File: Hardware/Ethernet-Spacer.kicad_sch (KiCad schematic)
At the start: 13 parts, among them J1 Conn_01x07_Male, J10 Conn_01x02_Male, J11 Conn_01x02_Male, J2 Conn_01x04_Male, J3 Conn_01x02_Male, J4 Conn_01x02_Male, J5 Conn_01x02_Male, J6 Conn_01x02_Male, J7 Conn_01x08_Male, J9 QWIIC_Stackable

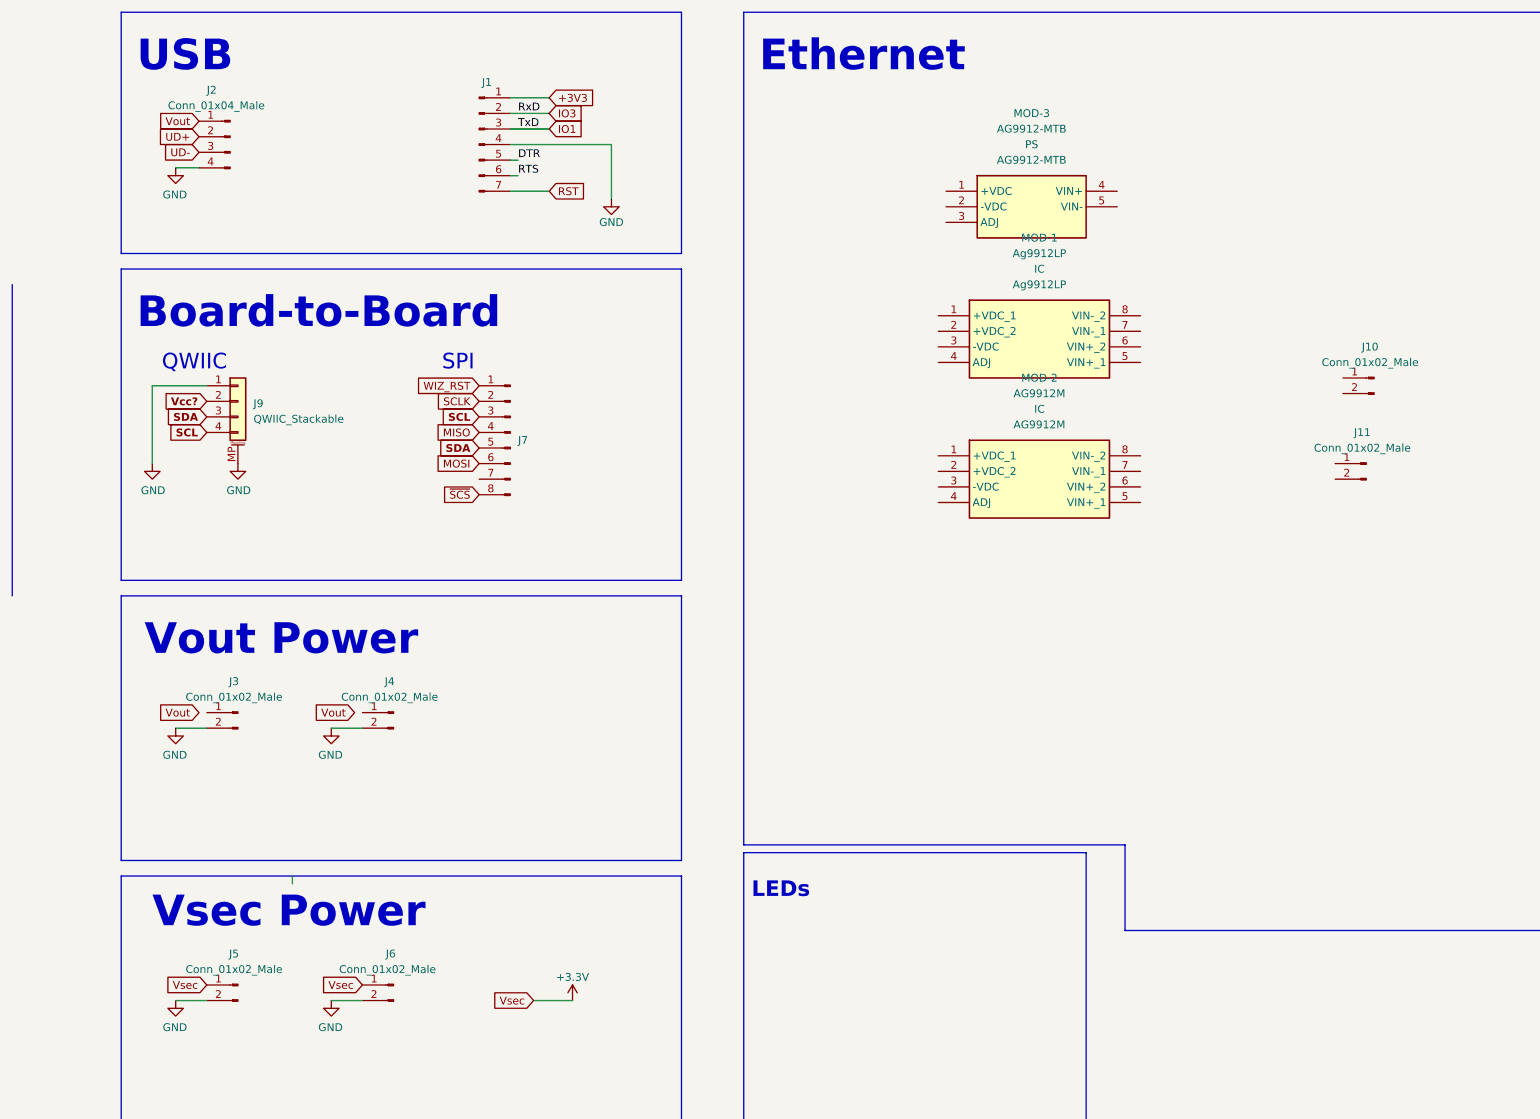
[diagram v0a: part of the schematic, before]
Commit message: Still working on changes to J7/J9...
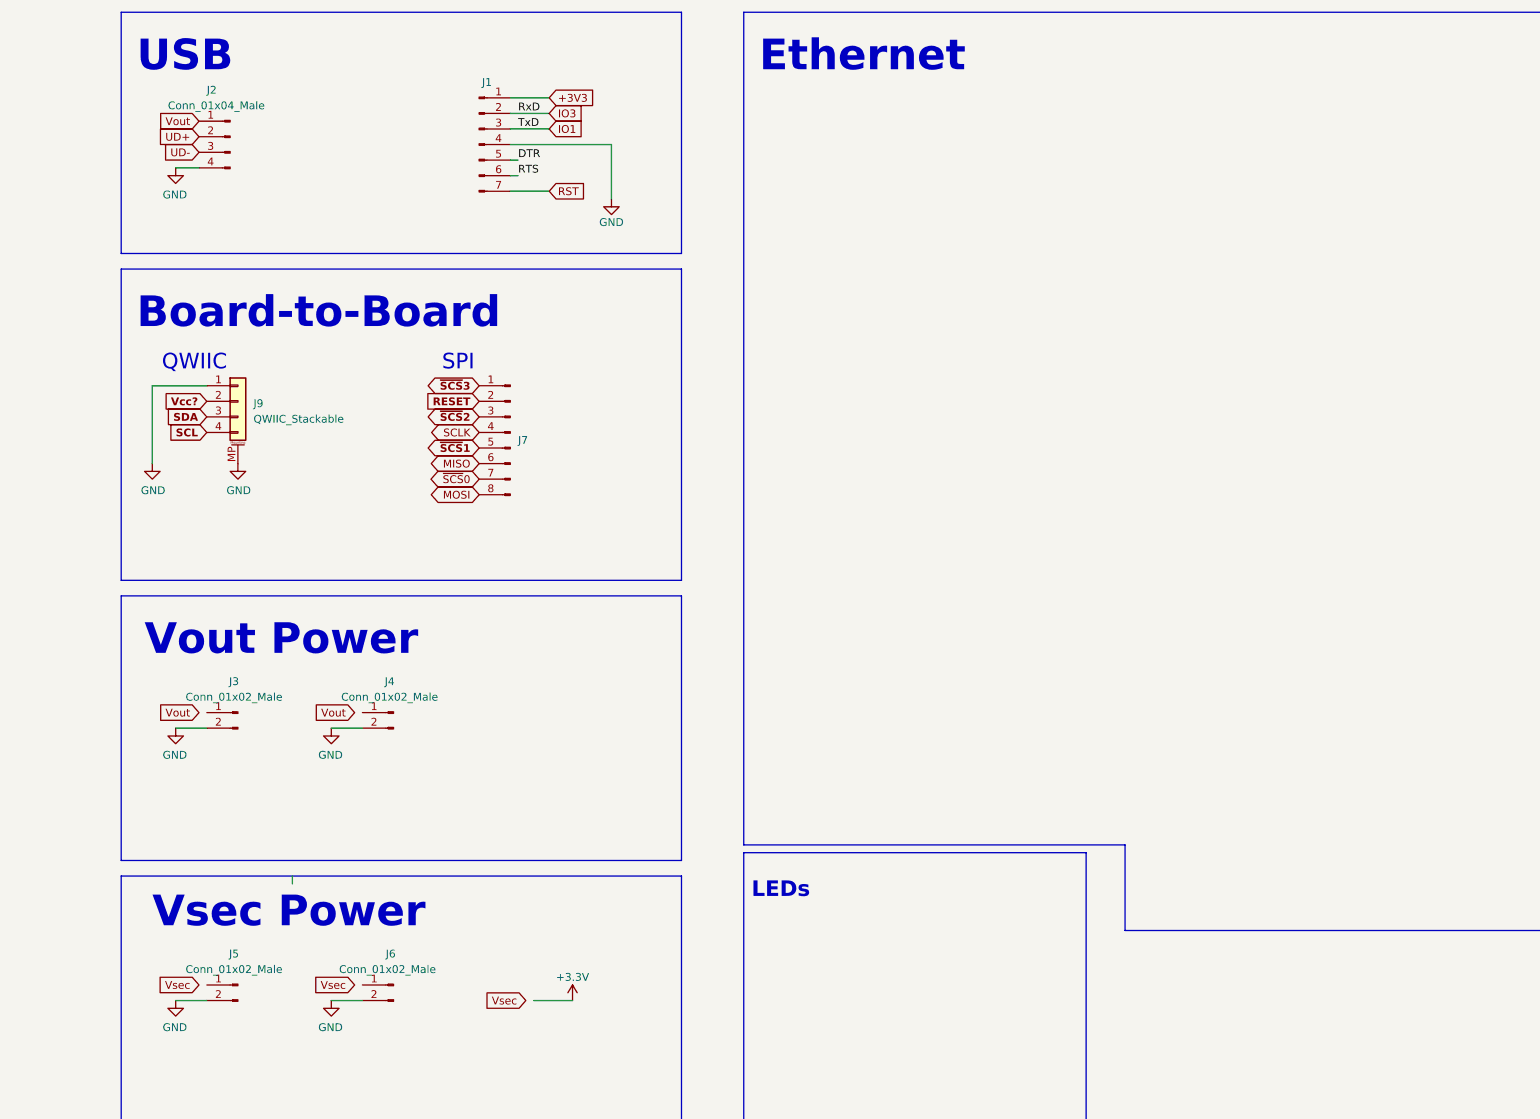
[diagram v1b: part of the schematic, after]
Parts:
- removed J10, J11: Conn_01x02_Male, Tinker:Board_Stacker_2, symbol Connector:Conn_01x02_Male
- removed MOD-1: Ag9912LP, symbol Ag9912LP:Ag9912LP
- removed MOD-2: AG9912M, symbol AG9912M:AG9912M
- removed MOD-3: AG9912-MTB, symbol AG9912-MTB:AG9912-MTB
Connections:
- net ~{SCS} is gone; now on net MOSI: J7.8 (Pin_8)
- net +3.3V: no longer J5.1 (Pin_1), J6.1 (Pin_1)
- net MISO: now also J7.6 (Pin_6); no longer J7.4 (Pin_4)
- net MOSI: no longer J7.6 (Pin_6)
- net SCL: no longer J7.3 (Pin_3)
- net SCLK: now also J7.4 (Pin_4); no longer J7.2 (Pin_2)
- net SDA: no longer J7.5 (Pin_5)
- net ~{SCS}0: now reaches J7.7 (Pin_7)
- net WIZ_RST renamed ~{SCS}3
- new net RESET: J7.2 (Pin_2)
- new net ~{SCS}1: J7.5 (Pin_5)
- new net ~{SCS}2: J7.3 (Pin_3)
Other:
- title: POE Spacer -> Ethernet Spacer

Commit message: Still migrating to 0.2.x
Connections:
- net ~{SCS}3 renamed ~{RESET}
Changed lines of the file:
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@@
+    )
+  )
+  (global_label "~{RESET}" (shape input) (at 72.39 74.93 180) (fields_autoplaced)
+    (effects (font (size 1.27 1.27) (thickness 0.254) bold) (justify right))
+    (property "Intersheet References" "${INTERSHEET_REFS}" (id 0) (at 64.0413 74.803 0)
+      (effects (font (size 1.27 1.27) (thickness 0.254) bold) (justify right) hide)
     )
   )
@@
     )
   )
-  (global_label "~{SCS}3" (shape bidirectional) (at 72.39 74.93 180) (fields_autoplaced)
-    (effects (font (size 1.27 1.27) (thickness 0.254) bold) (justify right))
-    (property "Intersheet References" "${INTERSHEET_REFS}" (id 0) (at 64.8879 74.803 0)
-      (effects (font (size 1.27 1.27) (thickness 0.254) bold) (justify right) hide)
-    )
-  )
